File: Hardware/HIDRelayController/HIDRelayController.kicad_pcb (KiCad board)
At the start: 2 copper layers, 45.7 x 30 mm, 19 parts, among them J1 Conn_01x04_Female, J2 Conn_01x11_Female, J3 USB_B_Micro, J4 AVR-ISP-6, U2 ATtiny261A-S, U3 ULN2803A, Y1 12MHz

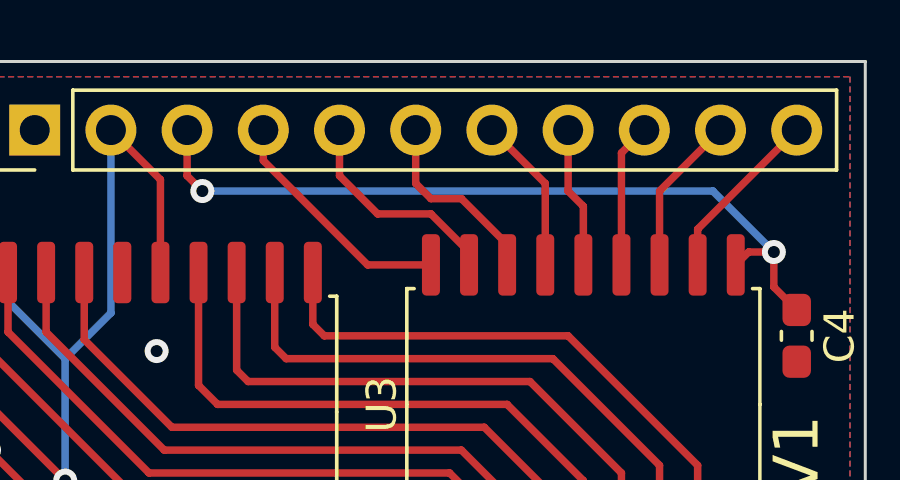
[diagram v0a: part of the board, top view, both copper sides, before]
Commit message: hardware: HIDRelayController: Remove silly via
No point in having a via for VRELAY right next to the PTH
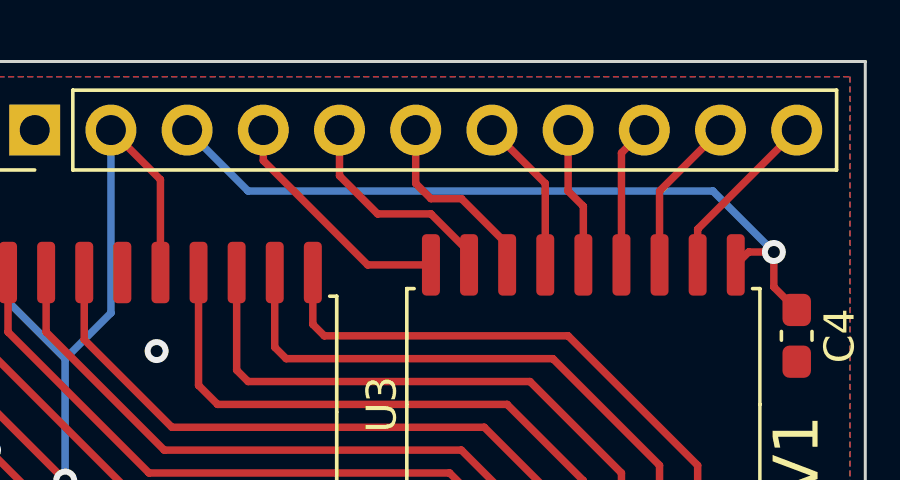
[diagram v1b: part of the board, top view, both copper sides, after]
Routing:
- net /VRELAY: track 25.8 -> 24.9 mm, vias 2 -> 1
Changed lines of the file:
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@@
   (segment (start 122.13 128.27) (end 125.0715 131.2115) (width 0.2) (layer "F.Cu") (net 10))
   (segment (start 148.449 124.714) (end 150.9795 124.714) (width 0.25) (layer "F.Cu") (net 11))
-  (segment (start 138.684 107.442) (end 138.684 108.966) (width 0.25) (layer "F.Cu") (net 12))
   (segment (start 158.242 111.506) (end 158.242 112.6755) (width 0.25) (layer "F.Cu") (net 12))
-  (segment (start 138.684 108.966) (end 139.192 109.474) (width 0.25) (layer "F.Cu") (net 12))
   (segment (start 158.242 111.506) (end 157.402 111.506) (width 0.25) (layer "F.Cu") (net 12))
   (segment (start 157.402 111.506) (end 156.972 111.936) (width 0.25) (layer "F.Cu") (net 12))
   (segment (start 158.242 112.6755) (end 159.004 113.4375) (width 0.25) (layer "F.Cu") (net 12))
   (via (at 158.242 111.506) (size 0.8) (drill 0.4) (layers "F.Cu" "B.Cu") (net 12))
-  (via (at 139.192 109.474) (size 0.8) (drill 0.4) (layers "F.Cu" "B.Cu") (net 12))
-  (segment (start 139.192 109.474) (end 156.21 109.474) (width 0.25) (layer "B.Cu") (net 12))
+  (segment (start 140.716 109.474) (end 138.684 107.442) (width 0.25) (layer "B.Cu") (net 12))
+  (segment (start 156.21 109.474) (end 140.716 109.474) (width 0.25) (layer "B.Cu") (net 12))
   (segment (start 156.21 109.474) (end 158.242 111.506) (width 0.25) (layer "B.Cu") (net 12))
   (segment (start 140.335 124.2375) (end 145.6375 129.54) (width 0.25) (layer "F.Cu") (net 13))
